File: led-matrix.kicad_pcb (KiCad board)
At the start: 2 copper layers, 86 x 46.5 mm, 128 parts

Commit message: finished small design for testing, now sending to university pcb for fabrication
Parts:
- added U1: ~, Connector_PinHeader_2.54mm:PinHeader_1x08_P2.54mm_Vertical, F.Cu at (152.5, 62.5)
- added U2: ~, Connector_PinHeader_2.54mm:PinHeader_1x16_P2.54mm_Vertical, F.Cu at (90.4, 81.0)
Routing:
- net Net-(D1-K): track 35.0 -> 55.7 mm
- net Net-(D114-K): track 35.0 -> 53.6 mm
- net Net-(D1-A): track 69.9 -> 88.5 mm
- net Net-(D112-K): track 35.0 -> 53.6 mm
- net Net-(D111-K): track 35.0 -> 52.2 mm
- net Net-(D115-K): track 35.0 -> 51.5 mm
- net Net-(D17-A): track 69.9 -> 85.3 mm
- net Net-(D110-K): track 35.0 -> 49.9 mm
- net Net-(D113-A): track 69.9 -> 84.8 mm
- net Net-(D100-K): track 35.0 -> 49.3 mm
- net Net-(D101-K): track 35.0 -> 47.6 mm
- net Net-(D109-K): track 35.0 -> 47.6 mm
- net Net-(D102-K): track 35.0 -> 46.7 mm
- net Net-(D108-K): track 35.0 -> 46.7 mm
- net Net-(D100-A): track 69.9 -> 81.1 mm
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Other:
- board size 86 x 46.5 mm -> 84 x 50 mm

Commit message: finished small design for testing, now sending to university pcb for fabrication
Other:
- board size 84 x 50 mm -> 86.5 x 52.5 mm
- board text added: "Alexander Holden Student id: 14264982"
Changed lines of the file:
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@@
 			(outputformat 1)
 			(mirror no)
-			(drillshape 1)
+			(drillshape 0)
 			(scaleselection 1)
-			(outputdirectory "")
+			(outputdirectory "gerber/")
 		)
 	)
@@
 	)
 	(gr_rect
-		(start 71.5 33.5)
-		(end 155.5 83.5)
+		(start 70 33)
+		(end 156.5 85.5)
 		(stroke
 			(width 0.05)
@@
 		(layer "Edge.Cuts")
 	)
+	(gr_text "Alexander Holden\nStudent id: 14264982"
+		(at 138 82 0)
+		(layer "F.SilkS")
+		(effects
+			(font
+				(size 1 1)
+				(thickness 0.1)
+			)
+			(justify left bottom)
+		)
+	)
 	(via

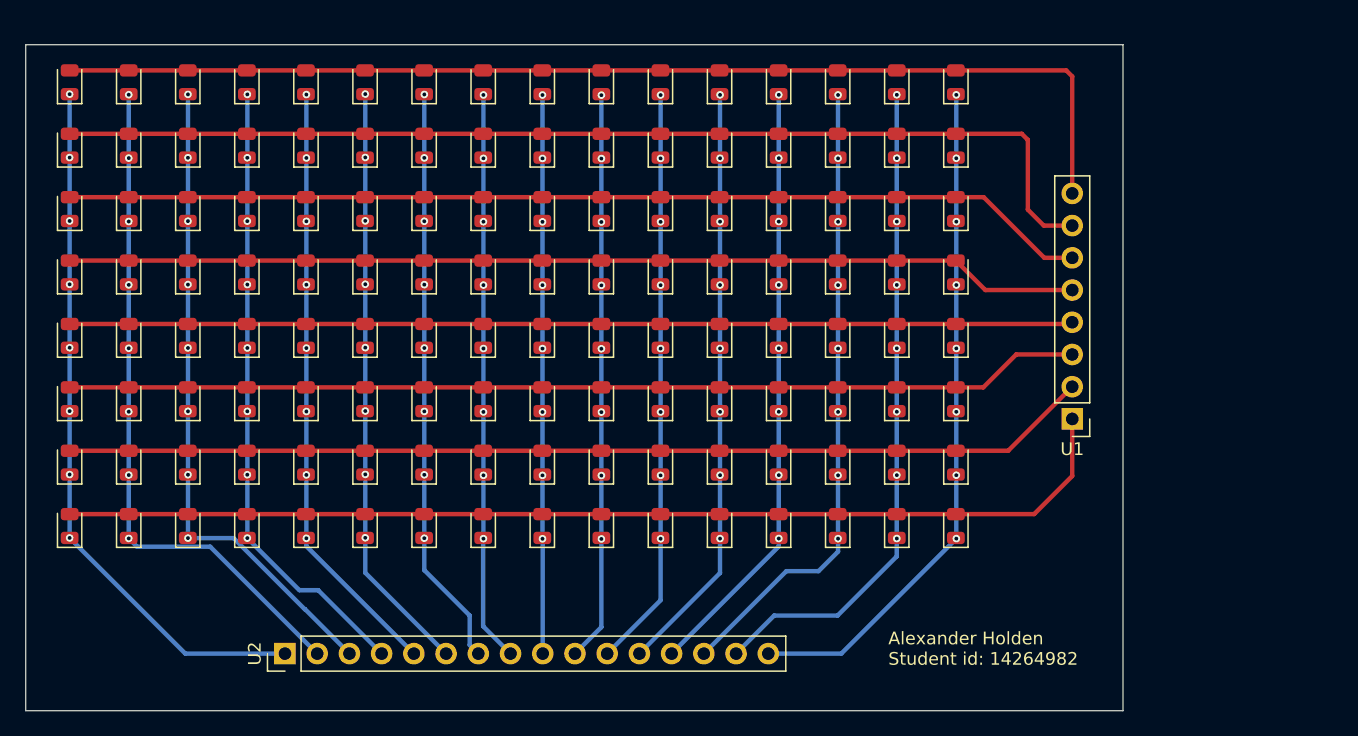
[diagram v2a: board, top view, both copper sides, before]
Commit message: added resistors to rows
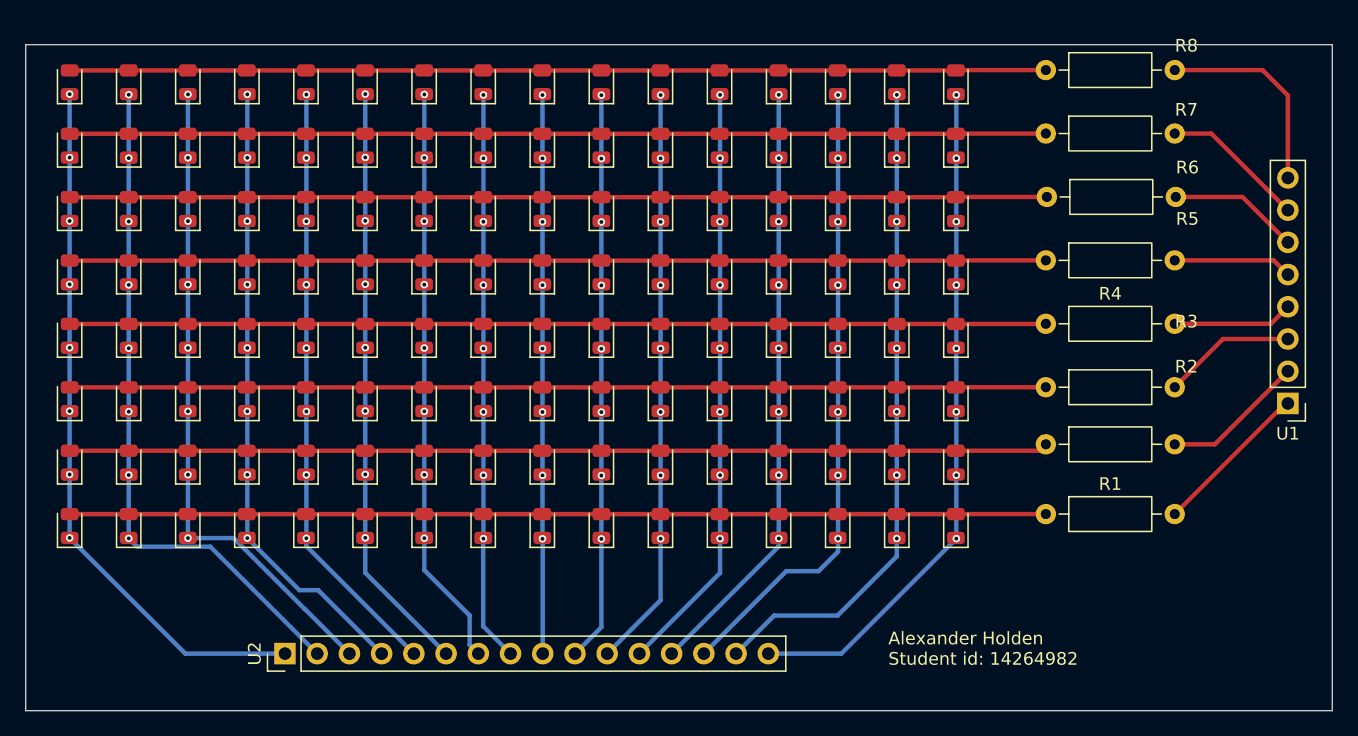
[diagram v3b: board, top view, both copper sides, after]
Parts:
- added R1: R, Resistor_THT:R_Axial_DIN0207_L6.3mm_D2.5mm_P10.16mm_Horizontal, F.Cu at (150.4, 70.0)
- added R2: R, Resistor_THT:R_Axial_DIN0207_L6.3mm_D2.5mm_P10.16mm_Horizontal, F.Cu at (150.4, 64.5)
- added R3: R, Resistor_THT:R_Axial_DIN0207_L6.3mm_D2.5mm_P10.16mm_Horizontal, F.Cu at (150.4, 60.0)
- added R4: R, Resistor_THT:R_Axial_DIN0207_L6.3mm_D2.5mm_P10.16mm_Horizontal, F.Cu at (150.4, 55.0)
- added R5: R, Resistor_THT:R_Axial_DIN0207_L6.3mm_D2.5mm_P10.16mm_Horizontal, F.Cu at (150.4, 50.0)
- added R6: R, Resistor_THT:R_Axial_DIN0207_L6.3mm_D2.5mm_P10.16mm_Horizontal, F.Cu at (150.5, 45.0)
- added R7: R, Resistor_THT:R_Axial_DIN0207_L6.3mm_D2.5mm_P10.16mm_Horizontal, F.Cu at (150.4, 40.0)
- added R8: R, Resistor_THT:R_Axial_DIN0207_L6.3mm_D2.5mm_P10.16mm_Horizontal, F.Cu at (150.4, 35.0)
- moved U1 17.0 mm to (169.5, 61.3)
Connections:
- U1 pad 1: Net-(D113-A) -> Net-(R1-Pad2)
- U1 pad 2: Net-(D100-A) -> Net-(R2-Pad2)
- U1 pad 3: Net-(D81-A) -> Net-(R3-Pad2)
- U1 pad 4: Net-(D65-A) -> Net-(R4-Pad2)
- U1 pad 5: Net-(D49-A) -> Net-(R5-Pad2)
- U1 pad 6: Net-(D33-A) -> Net-(R6-Pad2)
- U1 pad 7: Net-(D17-A) -> Net-(R7-Pad2)
- U1 pad 8: Net-(D1-A) -> Net-(R8-Pad2)
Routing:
- net Net-(R8-Pad2): track 0.00 -> 16.2 mm
- net Net-(R1-Pad2): track 0.00 -> 12.5 mm
- net Net-(D1-A): track 88.5 -> 77.0 mm
- net Net-(R7-Pad2): track 0.00 -> 11.4 mm
- net Net-(R2-Pad2): track 0.00 -> 11.3 mm
- net Net-(R3-Pad2): track 0.00 -> 10.5 mm
- net Net-(R6-Pad2): track 0.00 -> 10.3 mm
- net Net-(R4-Pad2): track 0.00 -> 9.48 mm
- net Net-(R5-Pad2): track 0.00 -> 9.38 mm
- net Net-(D17-A): track 85.3 -> 77.0 mm
- net Net-(D113-A): track 84.8 -> 77.0 mm
- net Net-(D33-A): track 81.0 -> 77.0 mm
- net Net-(D100-A): track 81.1 -> 77.2 mm
- net Net-(D81-A): track 80.1 -> 77.0 mm
- net Net-(D49-A): track 80.0 -> 77.0 mm
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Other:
- board size 86.5 x 52.5 mm -> 103 x 52.5 mm

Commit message: made slight adjustments
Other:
- board size 103 x 52.5 mm -> 102.5 x 53 mm
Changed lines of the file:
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@@
 		(tags "Resistor Axial_DIN0207 series Axial Horizontal pin pitch 10.16mm 0.25W = 1/4W length 6.3mm diameter 2.5mm")
 		(property "Reference" "R8"
-			(at 11.08 -1.92 0)
+			(at 5.08 -2.5 0)
 			(layer "F.SilkS")
+			(hide yes)
 			(effects
 				(font
@@
 			(at 11.08 -1.87 0)
 			(layer "F.SilkS")
+			(hide yes)
 			(effects
 				(font
@@
 			(at 11.16 -3.27 0)
 			(layer "F.SilkS")
+			(hide yes)
 			(effects
 				(font
@@
 			(at 11.08 -6.12 0)
 			(layer "F.SilkS")
+			(hide yes)
 			(effects
 				(font
@@
 			(at 0 -2.38 90)
 			(layer "F.SilkS")
+			(hide yes)
 			(effects
 				(font
@@
 			(at 11.08 -5.17 0)
 			(layer "F.SilkS")
+			(hide yes)
 			(effects
 				(font
@@
 			(at 5.08 -2.37 0)
 			(layer "F.SilkS")
+			(hide yes)
 			(effects
 				(font
@@
 			(at 5.08 -2.37 0)
 			(layer "F.SilkS")
+			(hide yes)
 			(effects
 				(font
@@
 			(at 11.08 -2.32 0)
 			(layer "F.SilkS")
+			(hide yes)
 			(effects
 				(font
@@
 			(at 0 2.5 0)
 			(layer "F.Fab")
+			(hide yes)
 			(effects
 				(font
@@
 			(at 0 -2.38 0)
 			(layer "F.SilkS")
+			(hide yes)
 			(effects
 				(font
@@
 	)
 	(gr_rect
-		(start 70 33)
-		(end 173 85.5)
+		(start 70.5 31.5)
+		(end 173 84.5)
 		(stroke
 			(width 0.05)
@@
 	)
 	(gr_text "Alexander Holden\nStudent id: 14264982"
-		(at 138 82 0)
+		(at 147.5 79.5 0)
 		(layer "F.SilkS")
 		(effects
@@
 	)
 	(segment
-		(start 84.550804 72.570804)
-		(end 78.775082 72.570804)
+		(start 88.48 76.5)
+		(end 92.98 81)
 		(width 0.35)
 		(layer "B.Cu")
@@
 	)
 	(segment
-		(start 92.98 81)
-		(end 84.550804 72.570804)
+		(start 78.124553 71.920275)
+		(end 82.704278 76.5)
 		(width 0.35)
 		(layer "B.Cu")
@@
 	)
 	(segment
-		(start 78.124553 71.920275)
-		(end 78.124553 36.941275)
+		(start 82.704278 76.5)
+		(end 88.48 76.5)
 		(width 0.35)
 		(layer "B.Cu")
@@
 	)
 	(segment
-		(start 78.775082 72.570804)
-		(end 78.124553 71.920275)
+		(start 78.124553 71.920275)
+		(end 78.124553 36.941275)
 		(width 0.35)
 		(layer "B.Cu")
@@
 	)
 	(segment
+		(start 88.5 75)
+		(end 91 77.5)
+		(width 0.35)
+		(layer "B.Cu")
+		(net 16)
+	)
+	(segment
 		(start 82.792157 71.894804)
-		(end 86.394804 71.894804)
+		(end 84.394804 71.894804)
+		(width 0.35)
+		(layer "B.Cu")
+		(net 16)
+	)
+	(segment
+		(start 84.394804 71.894804)
+		(end 87.5 75)
 		(width 0.35)
 		(layer "B.Cu")
@@
 	)
 	(segment
-		(start 92 77.5)
-		(end 92.02 77.5)
+		(start 87.5 75)
+		(end 88.5 75)
 		(width 0.35)
 		(layer "B.Cu")
@@
 	)
 	(segment
-		(start 86.394804 71.894804)
-		(end 92 77.5)
+		(start 91 77.5)
+		(end 92.02 77.5)
 		(width 0.35)
 		(layer "B.Cu")
